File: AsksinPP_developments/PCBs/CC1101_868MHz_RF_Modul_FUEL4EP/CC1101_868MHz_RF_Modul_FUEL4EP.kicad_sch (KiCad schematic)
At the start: 39 parts, among them U1 CC1101RGPR, Y1 Crystal 26MHz

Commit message: PCBs: CC1101_868MHz_RF_Modul_FUEL4EP: Improved decoupling by shorter return paths for GND loops
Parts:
- C13: footprint Capacitor_SMD:C_0402_1005Metric -> Capacitor_SMD:C_0603_1608Metric; LCSC C1525 -> C14663; TYPE 0402 -> 0603
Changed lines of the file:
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@@
   (title_block
     (title "CC1101_868MHz_RF_Modul_FUEL4EP")
-    (date "2023-08-28")
-    (rev "1.1")
+    (date "2023-09-21")
+    (rev "1.2")
     (company "(C) FUEL4EP 2023")
     (comment 1 "fork of Jérômes CC1101_module https://github.com/jp112sdl/CC1101_Module ")
@@
       (effects (font (size 1.27 1.27)) (justify left))
     )
-    (property "Footprint" "Capacitor_SMD:C_0402_1005Metric" (id 2) (at 64.4652 39.37 0)
+    (property "Footprint" "Capacitor_SMD:C_0603_1608Metric" (id 2) (at 64.4652 39.37 0)
       (effects (font (size 1.27 1.27)) hide)
     )
@@
       (effects (font (size 1.27 1.27)) hide)
     )
-    (property "LCSC" "C1525" (id 4) (at 63.5 35.56 0)
-      (effects (font (size 1.524 1.524)) hide)
-    )
-    (property "TYPE" "0402" (id 5) (at 63.5 35.56 0)
+    (property "LCSC" "C14663" (id 4) (at 63.5 35.56 0)
+      (effects (font (size 1.524 1.524)) hide)
+    )
+    (property "TYPE" "0603" (id 5) (at 63.5 35.56 0)
       (effects (font (size 1.524 1.524)) hide)
     )
@@
     )
     (path "/4511b598-0f07-476e-9b94-351960102c21"
-      (reference "C13") (unit 1) (value "100n") (footprint "Capacitor_SMD:C_0402_1005Metric")
+      (reference "C13") (unit 1) (value "100n") (footprint "Capacitor_SMD:C_0603_1608Metric")
     )
     (path "/05443561-7493-4e53-b694-85a09d97aade"

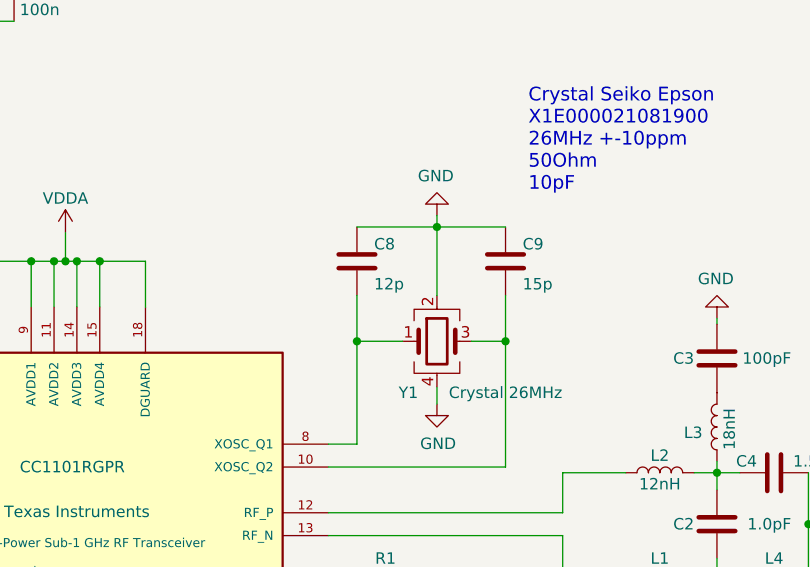
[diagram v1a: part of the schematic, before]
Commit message: PCBs: CC1101_868MHz_RF_Modul_FUEL4EP and CC1101_868MHz_UFL_RF_Modul_FUEL4EP: Reduction of parasitic capaitance of oscillator layout; use 1% CoG capacitors for oscillator
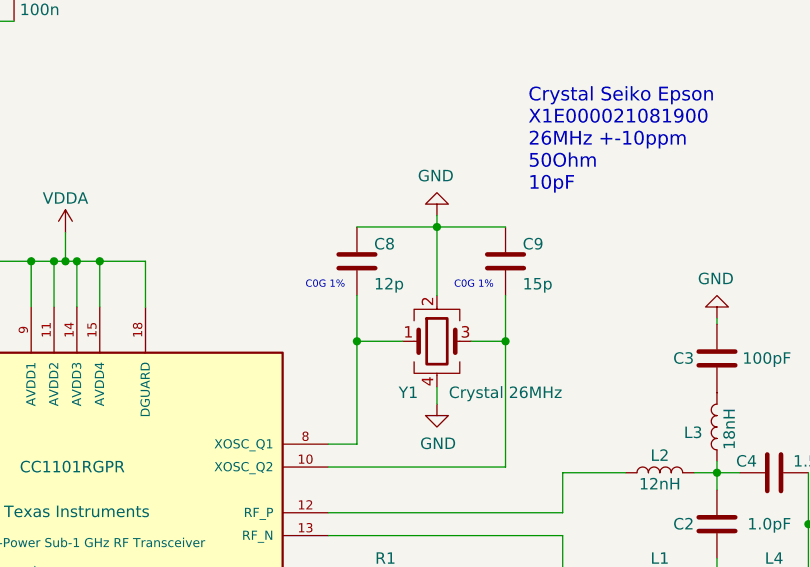
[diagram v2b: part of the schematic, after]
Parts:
- C8: LCSC C1547 -> C393682; Remark (none) -> use C0G ±1% type!
- C9: LCSC C2169087 -> C441742; Remark (none) -> use C0G ±1% type!
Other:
- note added: "C0G 1%"
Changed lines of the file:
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@@
   (title_block
     (title "CC1101_868MHz_RF_Modul_FUEL4EP")
-    (date "2023-09-21")
-    (rev "1.2")
+    (date "2023-09-29")
+    (rev "1.3")
     (company "(C) FUEL4EP 2023")
     (comment 1 "fork of Jérômes CC1101_module https://github.com/jp112sdl/CC1101_Module ")
@@
     (at 149.225 58.42 0)
     (effects (font (size 1.524 1.524)) (justify left bottom))
+  )
+  (text "C0G 1%" (at 140.97 69.215 0)
+    (effects (font (size 0.8 0.8)) (justify left bottom))
+  )
+  (text "C0G 1%" (at 124.46 69.215 0)
+    (effects (font (size 0.8 0.8)) (justify left bottom))
   )
   (label "MISO{slash}GDO1" (at 68.58 91.44 180)
@@
       (effects (font (size 1.27 1.27)) hide)
     )
-    (property "LCSC" "C1547" (id 4) (at 130.175 66.04 0)
+    (property "LCSC" "C393682" (id 4) (at 130.175 66.04 0)
       (effects (font (size 1.524 1.524)) hide)
     )
     (property "TYPE" "0402" (id 5) (at 130.175 66.04 0)
+      (effects (font (size 1.524 1.524)) hide)
+    )
+    (property "Remark" "use C0G ±1% type!" (id 6) (at 130.175 66.04 0)
       (effects (font (size 1.524 1.524)) hide)
     )
@@
       (effects (font (size 1.27 1.27)) hide)
     )
-    (property "LCSC" "C2169087" (id 4) (at 146.685 66.04 0)
+    (property "LCSC" "C441742" (id 4) (at 146.685 66.04 0)
       (effects (font (size 1.524 1.524)) hide)
     )
@@
       (effects (font (size 1.524 1.524)) hide)
     )
+    (property "Remark" "use C0G ±1%  type!" (id 6) (at 146.685 66.04 0)
+      (effects (font (size 1.524 1.524)) hide)
+    )

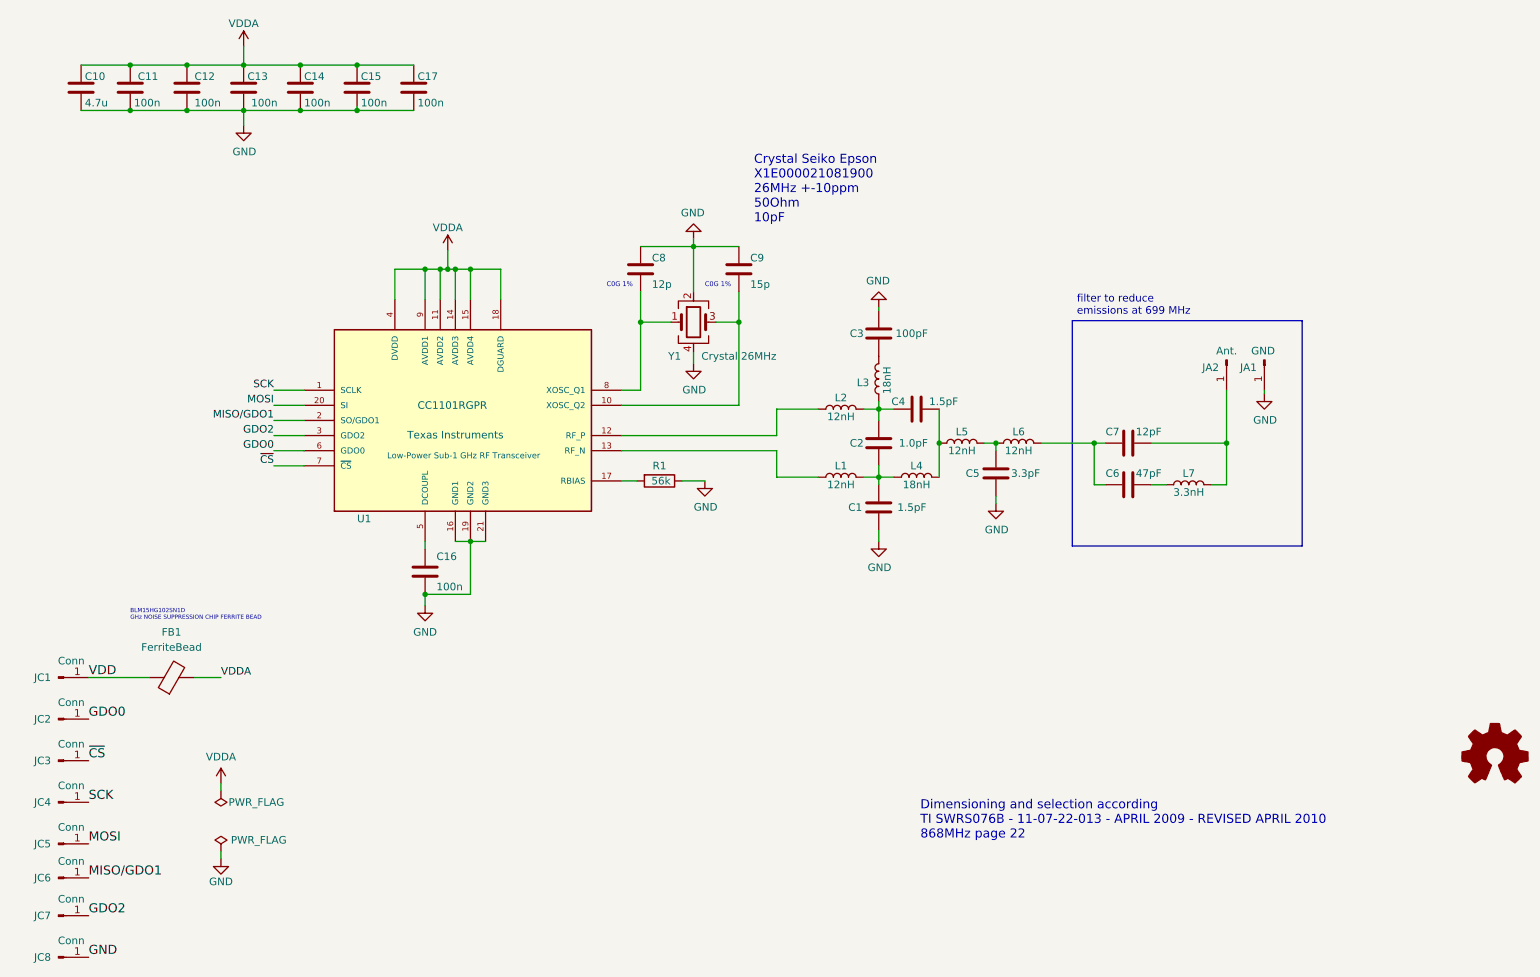
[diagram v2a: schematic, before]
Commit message: PCBs/CC1101_868MHz_RF_Modul_FUEL4EP: migration to KiCAD 8
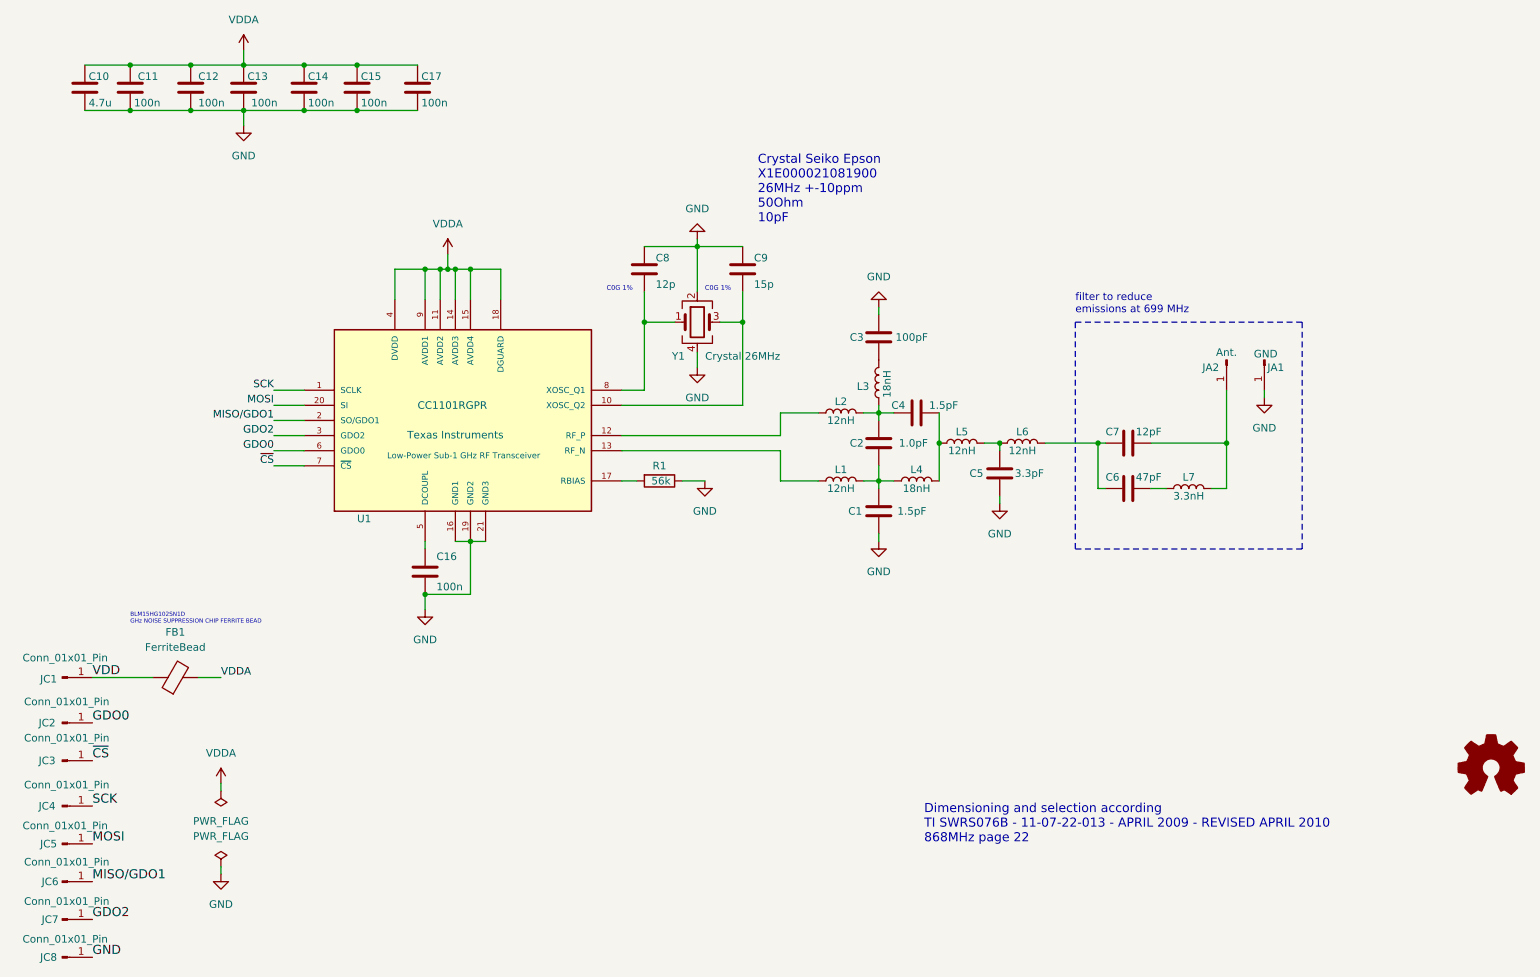
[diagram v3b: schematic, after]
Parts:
- removed JA1: GND, FUEL4EP:edge_hole_Pitch2.28mm_Drill0.8mm, symbol Connector:Conn_01x01_Male
- removed JA2: Ant., FUEL4EP:edge_hole_Pitch2.28mm_Drill0.8mm, symbol Connector:Conn_01x01_Male
- removed JC1: Conn, FUEL4EP:edge_hole_Pitch1.27mm_Drill0.75mm, symbol Connector:Conn_01x01_Male
- removed JC2, JC3, JC4, JC5, JC6, JC7, JC8: Conn, FUEL4EP:edge_hole_Pitch1.27mm_Drill0.75mm_rounded, symbol Connector:Conn_01x01_Male
- removed LOGO1: Logo_Open_Hardware_Small, FUEL4EP:CC-BY-ND-SA_bottom, symbol Graphic:Logo_Open_Hardware_Small
- added JA1: GND, FUEL4EP:edge_hole_Pitch1.27mm_Drill0.75mm, symbol Connector:Conn_01x01_Pin
- added JA2: Ant., FUEL4EP:edge_hole_Pitch1.27mm_Drill0.75mm, symbol Connector:Conn_01x01_Pin
- added JC1: Conn_01x01_Pin, FUEL4EP:edge_hole_Pitch1.27mm_Drill0.75mm, symbol Connector:Conn_01x01_Pin
- added JC2, JC3, JC4, JC5, JC6, JC7, JC8: Conn_01x01_Pin, FUEL4EP:edge_hole_Pitch1.27mm_Drill0.75mm_rounded, symbol Connector:Conn_01x01_Pin
- U1: footprint Package_DFN_QFN:Texas_S-PVQFN-N20_EP2.4x2.4mm_ThermalVias -> Package_DFN_QFN:Texas_RGP0020H_VQFN-20-1EP_4x4mm_P0.5mm_EP2.4x2.4mm_ThermalVias; Description_1 (none) -> Low-Power Sub-1 GHz RF Transceiver
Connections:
- net GDO0: now also JC2.1 (Pin_1)
- net GDO2: now also JC7.1 (Pin_1)
- net GND: now also JA1.1 (Pin_1), JC8.1 (Pin_1)
- net MISO/GDO1: now also JC6.1 (Pin_1)
- net MOSI: now also JC5.1 (Pin_1)
- net SCK: now also JC4.1 (Pin_1)
- net VDD: now also JC1.1 (Pin_1)
- net ~{CS}: now also JC3.1 (Pin_1)
- net at C7.1, L7.2: now also JA2.1 (Pin_1)
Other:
- moved on the sheet: C1, C10, C12, C14, C17, C3, C4, C5, C6, C8, C9, FB1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
